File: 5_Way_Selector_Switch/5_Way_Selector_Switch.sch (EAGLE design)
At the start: 7 parts

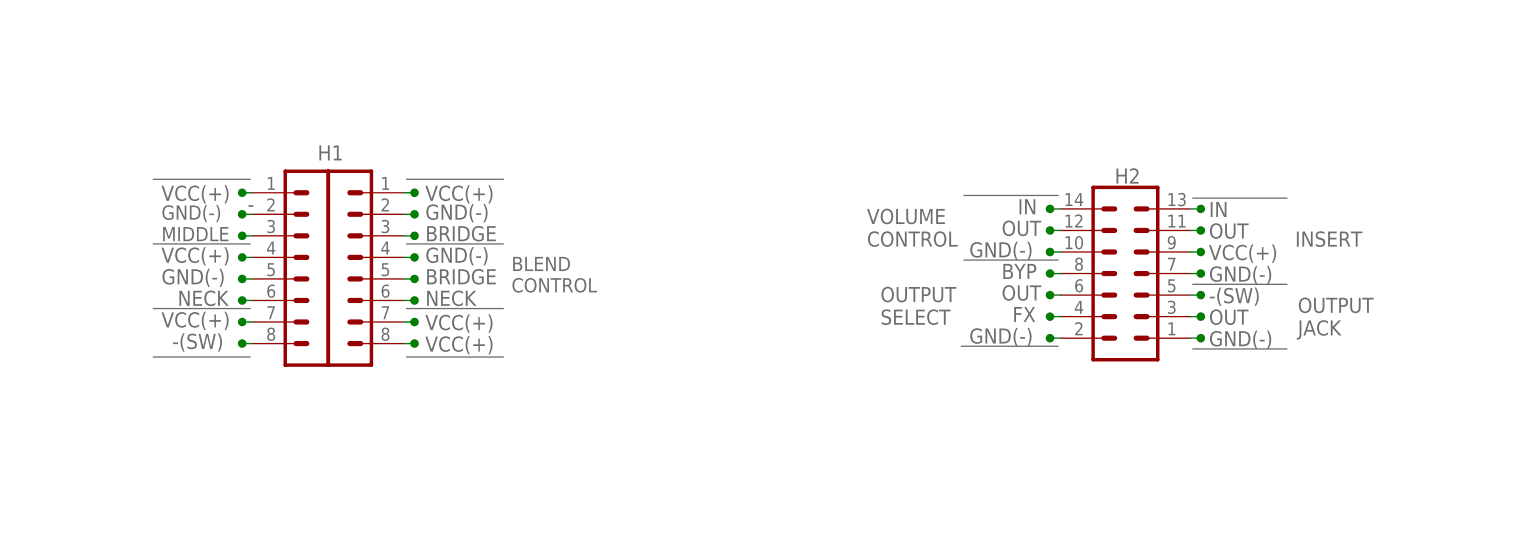
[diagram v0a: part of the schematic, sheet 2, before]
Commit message: Updates/ label modifications to make them consistent
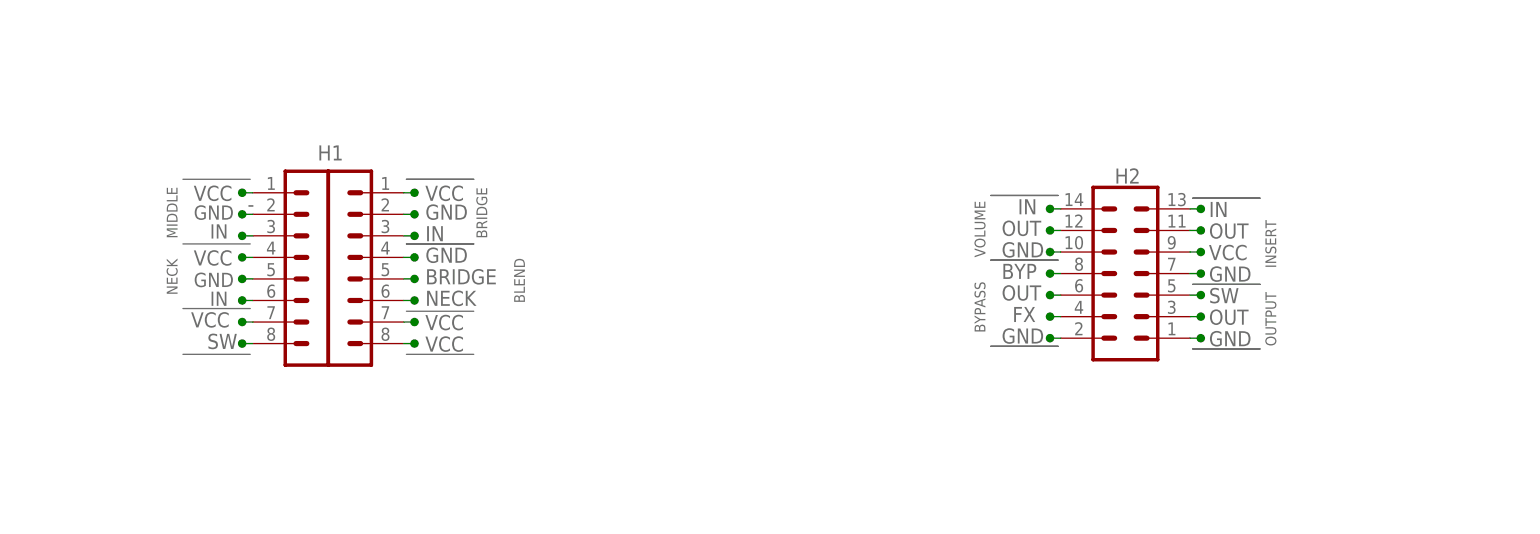
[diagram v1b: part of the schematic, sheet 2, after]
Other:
- note added: "BLEND"
- note added: "BYPASS"
- note added: "GND"
- note added: "OUTPUT"
- note added: "SW"
- note added: "VCC"
- note added: "VOLUME"
- note removed: "-(SW)"
- note removed: "ACTIVE PICKUP INPUTS"
- note removed: "BATT"
- note removed: "BLEND CONTROL"
- note removed: "GND(-)"
- note removed: "OUTPUT JACK"
- note removed: "OUTPUT SELECT"
- note removed: "VCC(+)"
- note removed: "VOLUME CONTROL"

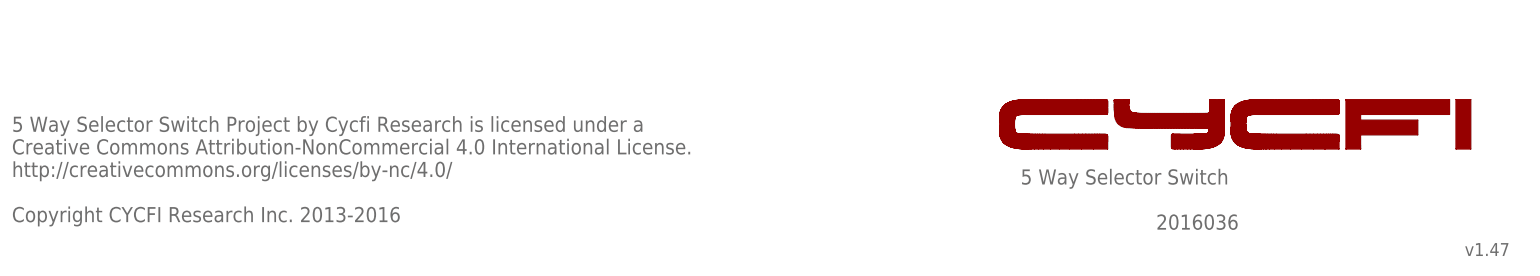
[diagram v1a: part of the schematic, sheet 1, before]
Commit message: Updated schematic licenses
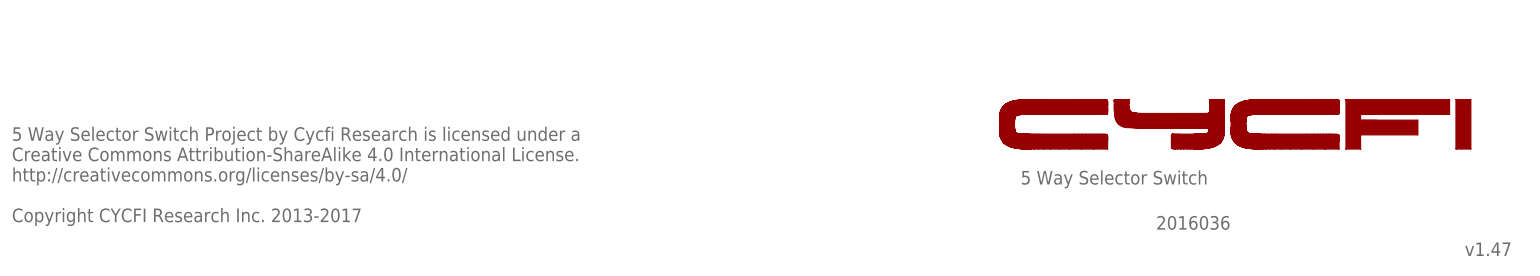
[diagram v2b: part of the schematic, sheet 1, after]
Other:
- note added: "5 Way Selector Switch Project by Cycfi Research is licensed under a Creative Commons Attribution-ShareAlike 4.0 International License. http://creativecommons.org/licenses/by-sa/4.0/ Copyright CYCFI Research Inc. 2013-2017"
- note removed: "5 Way Selector Switch Project by Cycfi Research is licensed under a Creative Commons Attribution-NonCommercial 4.0 International License. http://creativecommons.org/licenses/by-nc/4.0/ Copyright CYCFI Research Inc. 2013-2016"
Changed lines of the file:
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@@
 <setting verticaltext="up"/>
 </settings>
-<grid distance="0.0125" unitdist="inch" unit="inch" style="lines" multiple="1" display="yes" altdistance="0.01" altunitdist="inch" altunit="inch"/>
+<grid distance="0.1" unitdist="inch" unit="inch" style="lines" multiple="1" display="no" altdistance="0.01" altunitdist="inch" altunit="inch"/>
 <layers>
 <layer number="1" name="Top" color="4" fill="1" visible="no" active="no"/>
@@
 <text x="189.865" y="80.645" size="1.778" layer="95">OUTPUT </text>
 <text x="189.865" y="116.205" size="1.778" layer="95">BYPASS</text>
-<text x="177.8" y="19.05" size="2.54" layer="95">5 Way Selector Switch</text>
-<text x="252.73" y="6.985" size="2.1844" layer="95">v1.47</text>
-<text x="7.62" y="12.7" size="2.54" layer="95">5 Way Selector Switch Project by Cycfi Research is licensed under a
-Creative Commons Attribution-NonCommercial 4.0 International License.
-http://creativecommons.org/licenses/by-nc/4.0/
-Copyright CYCFI Research Inc. 2013-2016</text>
-<text x="200.66" y="11.43" size="2.54" layer="95">2016036</text>
+<text x="177.8" y="19.05" size="2.286" layer="95" font="fixed">5 Way Selector Switch</text>
+<text x="252.73" y="6.985" size="2.286" layer="95" font="fixed">v1.47</text>
+<text x="7.62" y="12.7" size="2.286" layer="95" font="fixed">5 Way Selector Switch Project by Cycfi Research is licensed under a
+Creative Commons Attribution-ShareAlike 4.0 International License.
+http://creativecommons.org/licenses/by-sa/4.0/
+Copyright CYCFI Research Inc. 2013-2017</text>
+<text x="200.66" y="11.43" size="2.286" layer="95" font="fixed">2016036</text>
 <wire x1="192.47528125" y1="25.047221875" x2="190.115640625" y2="25.047221875" width="0" layer="94"/>
 <wire x1="190.115640625" y1="25.047221875" x2="188.10833125" y2="25.047225" width="0" layer="94"/>
@@
 <instance part="FRAME1" gate="G$1" x="0" y="0"/>
 <instance part="FRAME1" gate="G$2" x="162.56" y="0" smashed="yes">
-<attribute name="LAST_DATE_TIME" x="175.26" y="1.27" size="2.54" layer="94" font="vector"/>
-<attribute name="SHEET" x="248.92" y="1.27" size="2.54" layer="94" font="vector"/>
+<attribute name="LAST_DATE_TIME" x="175.26" y="1.27" size="2.286" layer="94" font="vector"/>
+<attribute name="SHEET" x="248.92" y="1.27" size="2.286" layer="94" font="vector"/>
 </instance>
 </instances>
@@
 <text x="201.295" y="100.965" size="1.27" layer="95" rot="R90">INSERT</text>
 <text x="201.295" y="91.7575" size="1.27" layer="95" rot="R90">OUTPUT</text>
-<text x="177.8" y="19.05" size="2.54" layer="95">5 Way Selector Switch</text>
-<text x="252.73" y="6.985" size="2.1844" layer="95">v1.47</text>
-<text x="7.62" y="12.7" size="2.54" layer="95">5 Way Selector Switch Project by Cycfi Research is licensed under a
-Creative Commons Attribution-NonCommercial 4.0 International License.
-http://creativecommons.org/licenses/by-nc/4.0/
-Copyright CYCFI Research Inc. 2013-2016</text>
-<text x="200.66" y="11.43" size="2.54" layer="95">2016036</text>
+<text x="177.8" y="19.05" size="2.286" layer="95" font="vector">5 Way Selector Switch</text>
+<text x="252.73" y="6.985" size="2.286" layer="95" font="vector">v1.47</text>
+<text x="7.62" y="12.7" size="2.286" layer="95" font="vector">5 Way Selector Switch Project by Cycfi Research is licensed under a
+Creative Commons Attribution-ShareAlike 4.0 International License.
+http://creativecommons.org/licenses/by-sa/4.0/
+Copyright CYCFI Research Inc. 2013-2017</text>
+<text x="200.66" y="11.43" size="2.286" layer="95" font="vector">2016036</text>
 <wire x1="199.39" y1="91.44" x2="191.4525" y2="91.44" width="0.1524" layer="95"/>
 <wire x1="192.47528125" y1="25.047221875" x2="190.115640625" y2="25.047221875" width="0" layer="94"/>
